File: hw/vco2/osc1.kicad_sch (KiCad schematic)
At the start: 13 parts, among them U1 SSI2131

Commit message: Place components
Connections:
- net HARD_SYNC renamed ANTI_HANGUP
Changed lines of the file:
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@@
+	)
+	(junction
+		(at 160.02 95.25)
+		(diameter 0)
+		(color 0 0 0 0)
 	)
 	(junction
@@
 	(wire
 		(pts
-			(xy 156.21 95.25) (xy 161.29 95.25)
+			(xy 156.21 95.25) (xy 160.02 95.25)
 		)
 		(stroke
@@
 	(wire
 		(pts
+			(xy 160.02 95.25) (xy 161.29 95.25)
+		)
+		(stroke
+			(width 0)
+			(type default)
+		)
+	)
+	(wire
+		(pts
 			(xy 222.25 68.58) (xy 222.25 72.39)
 		)
@@
 	(wire
 		(pts
+			(xy 160.02 99.06) (xy 160.02 95.25)
+		)
+		(stroke
+			(width 0)
+			(type default)
+		)
+	)
+	(wire
+		(pts
 			(xy 156.21 83.82) (xy 177.8 83.82)
 		)
@@
 		(pts
 			(xy 121.92 99.06) (xy 128.27 99.06)
+		)
+		(stroke
+			(width 0)
+			(type default)
+		)
+	)
+	(wire
+		(pts
+			(xy 161.29 99.06) (xy 160.02 99.06)
 		)
 		(stroke
@@
 		)
 	)
+	(global_label "ANTI_HANGUP"
+		(shape input)
+		(at 161.29 99.06 0)
+		(fields_autoplaced yes)
+		(effects
+			(font
+				(size 1.27 1.27)
+			)
+			(justify left)
+		)
+		(property "Intersheetrefs" "${INTERSHEET_REFS}"
+			(at 176.8544 99.06 0)
+			(effects
+				(font
+					(size 1.27 1.27)
+				)
+				(justify left)
+				(hide yes)
+			)
+		)
+	)

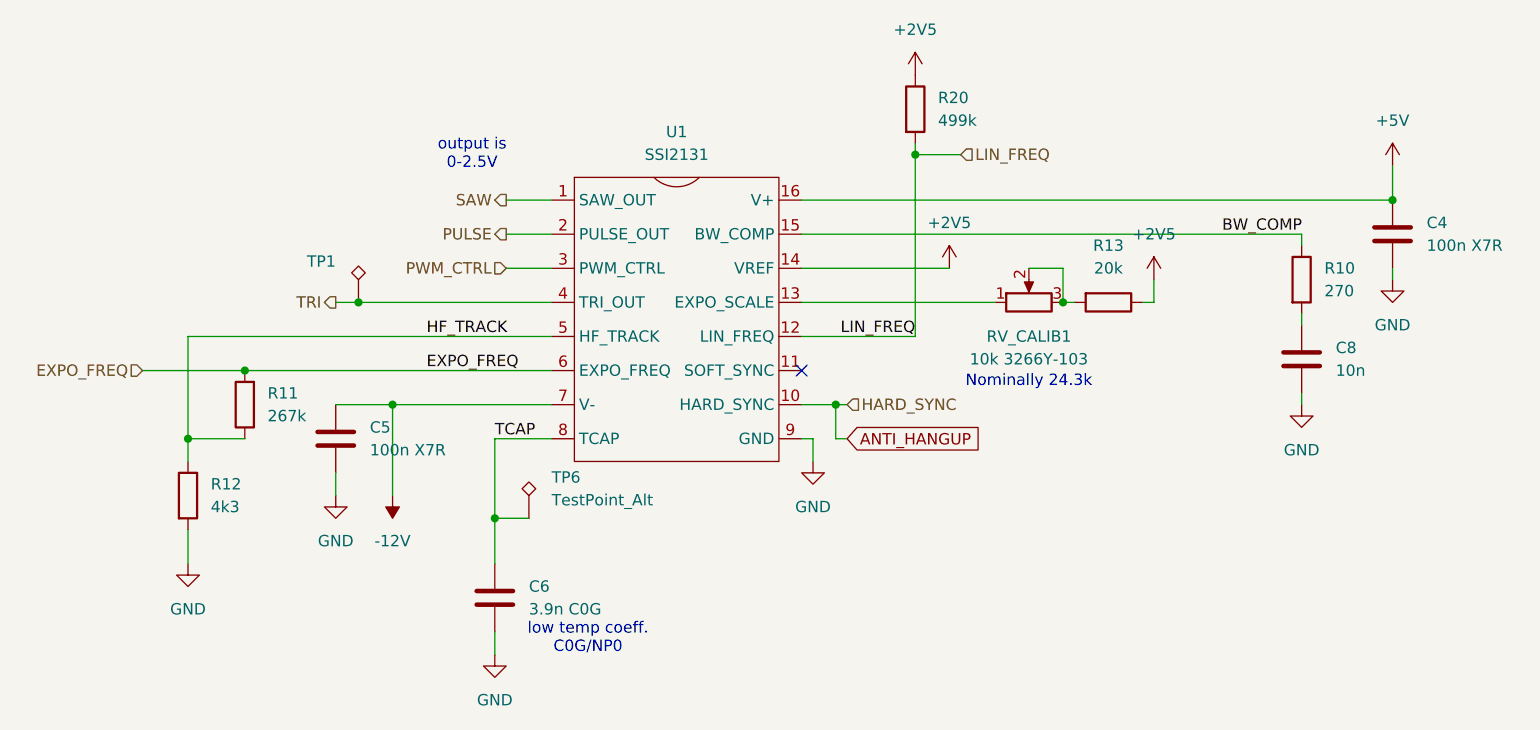
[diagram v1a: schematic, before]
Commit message: WIP: Redesign VCO2 board
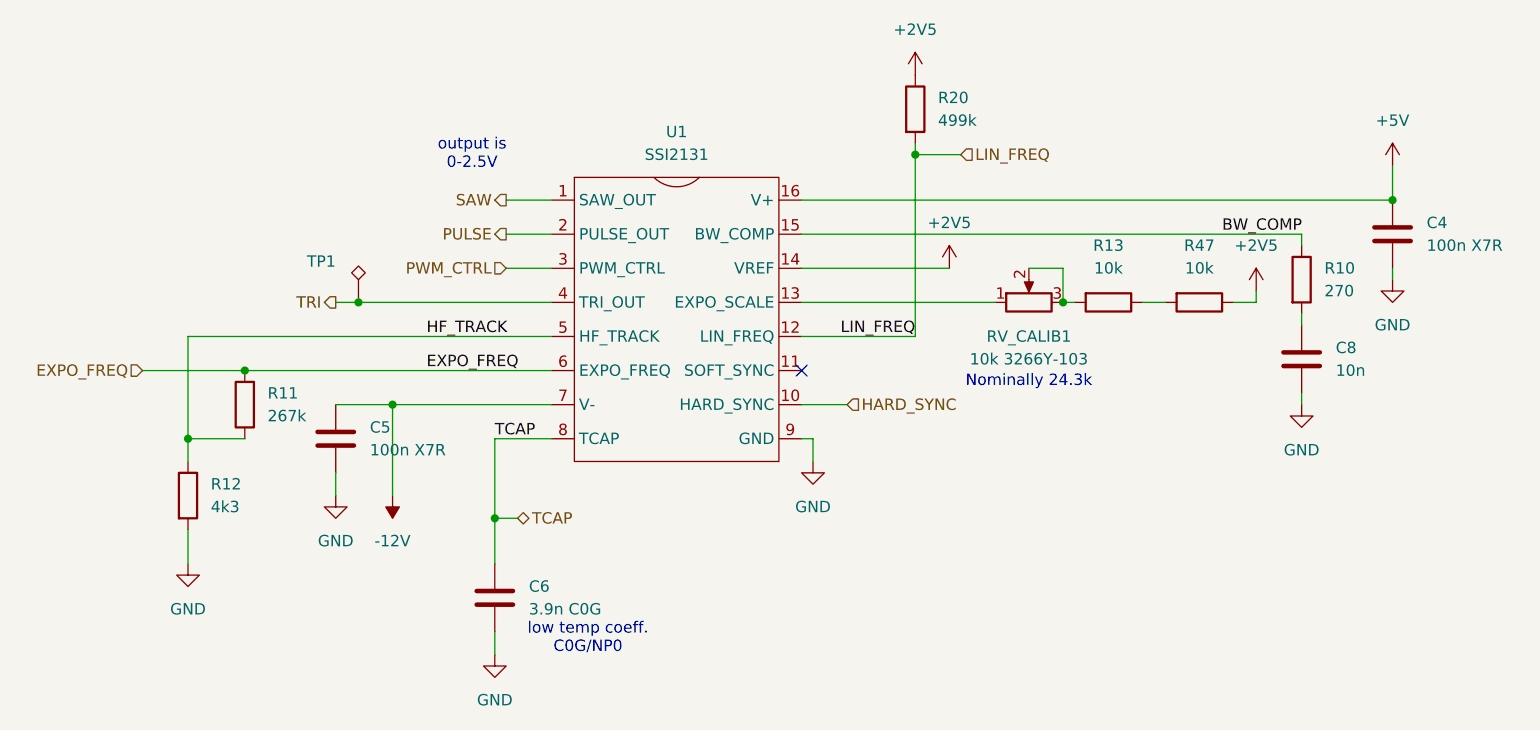
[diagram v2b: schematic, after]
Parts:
- removed TP6: TestPoint_Alt, Holes:TP_0.9mm, symbol Connector:TestPoint_Alt
- added R47: 10k, Resistor_SMD:R_0603_1608Metric, symbol Device:R
- C4, C5, C6, C8: footprint Capacitor_SMD:C_0603_1608Metric_Pad1.08x0.95mm_HandSolder -> Capacitor_SMD:C_0603_1608Metric
- R10, R11, R12, R20: footprint Resistor_SMD:R_0603_1608Metric_Pad0.98x0.95mm_HandSolder -> Resistor_SMD:R_0603_1608Metric
- R13: value 20k -> 10k; footprint Resistor_SMD:R_0603_1608Metric_Pad0.98x0.95mm_HandSolder -> Resistor_SMD:R_0603_1608Metric
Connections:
- net +2V5: now also R47.1; no longer R13.1
- net ANTI_HANGUP renamed HARD_SYNC
- new net: R13.1, R47.2

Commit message: VCO2 production work
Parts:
- U1: LCSC (none) -> C9900051822
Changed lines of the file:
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@@
+			)
+		)
+		(property "LCSC" "C9900051822"
+			(at 142.24 85.09 0)
+			(effects
+				(font
+					(size 1.27 1.27)
+				)
+				(hide yes)
 			)
 		)

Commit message: VCO2 rev 2 as sent for production at JLCPCB
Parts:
- C6: LCSC (none) -> C36911425
- R11: LCSC (none) -> C217914
- R13: LCSC (none) -> C95204
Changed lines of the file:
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@@
+			)
+		)
+		(property "LCSC" "C217914"
+			(at 93.98 95.25 0)
+			(effects
+				(font
+					(size 1.27 1.27)
+				)
+				(hide yes)
 			)
 		)
@@
 			)
 		)
+		(property "LCSC" "C95204"
+			(at 190.5 83.82 90)
+			(effects
+				(font
+					(size 1.27 1.27)
+				)
+				(hide yes)
+			)
+		)
 		(pin "2"
 		)
@@
 			(at 121.92 116.84 0)
 			(effects
+				(font
+					(size 1.27 1.27)
+				)
+				(hide yes)
+			)
+		)
+		(property "LCSC" "C36911425"
+			(at 121.92 116.84 0)
+			(effects
